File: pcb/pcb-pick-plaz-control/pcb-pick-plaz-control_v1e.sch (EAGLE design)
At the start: 202 parts, among them J1 USB-ID-THT, J3 USB-LCSC_C42431, J3C USB-LCSC_C42431, J3C1 USB-LCSC_C42431, U1 STM32F411VET6, U2 CH340, U3 TPS54227DDAR, U4 SL2.1A, U5 TPS54227DDAR, X1 04-JST-B4B-XH-A, X10 03-JST-B3B-XH-A, X11 03-JST-B3B-XH-A, X12 03-JST-B3B-XH-A, X13 02-JST-B3B-XH-A, X14 02-JST-B3B-XH-A, X15 02-JST-B3B-XH-A, X16 02-JST-B3B-XH-A, X17 02-JST-B3B-XH-A, X18 02-JST-B3B-XH-A, X19 05-JST-B5B-XH-A, X2 04-JST-B4B-XH-A, X20 05-JST-B5B-XH-A, X21 04-JST-B4B-XH-A, X22 PIN_2X13.81MM_LONGPAD, X23 02-JST-B3B-XH-A, X24 02-JST-B3B-XH-A, X25 04-JST-B4B-XH-A, X26 05-JST-B5B-XH-A, X27 05-JST-B5B-XH-A, X28 05-JST-B5B-XH-A, X29 02-JST-B3B-XH-A, X3 04-JST-B4B-XH-A, X30 02-JST-B3B-XH-A, X31 02-JST-B3B-XH-A, X32 02-JST-B3B-XH-A, X33 04-JST-B4B-XH-A, X4 04-JST-B4B-XH-A, X5 04-JST-B4B-XH-A, X6 04-JST-B4B-XH-A, X7 03-JST-B3B-XH-A, X8 03-JST-B3B-XH-A, X9 03-JST-B3B-XH-A, Y1 3213-QUARZ3225, Y2 3213-QUARZ3225, Y3 3213-QUARZ3225

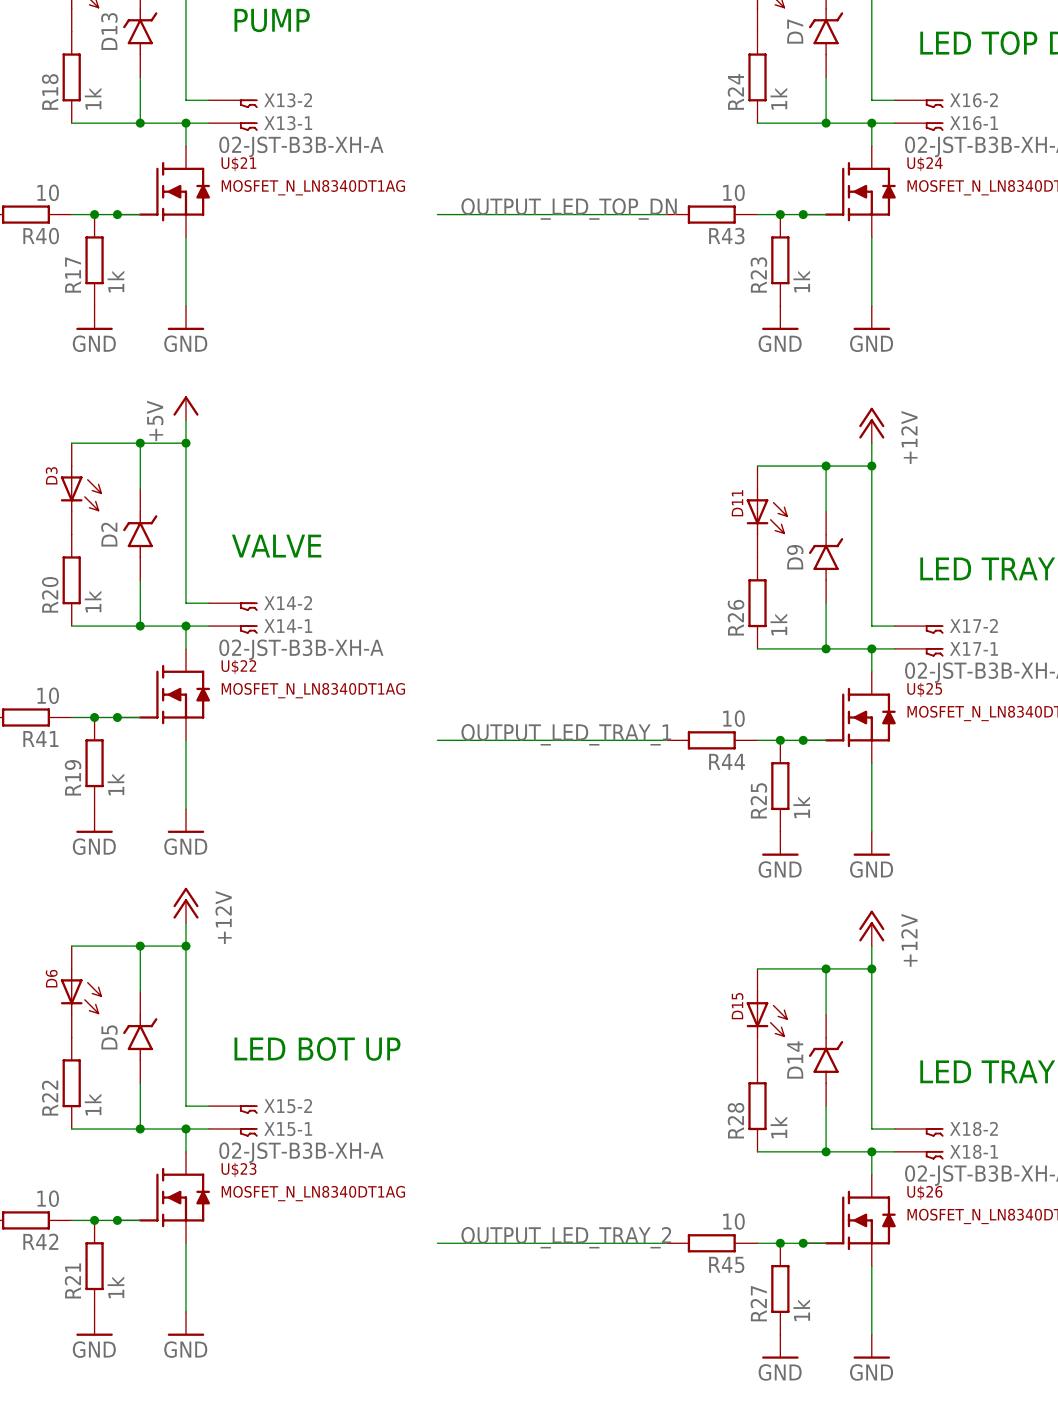
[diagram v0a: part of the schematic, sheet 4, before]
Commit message: updated pcbs with step files
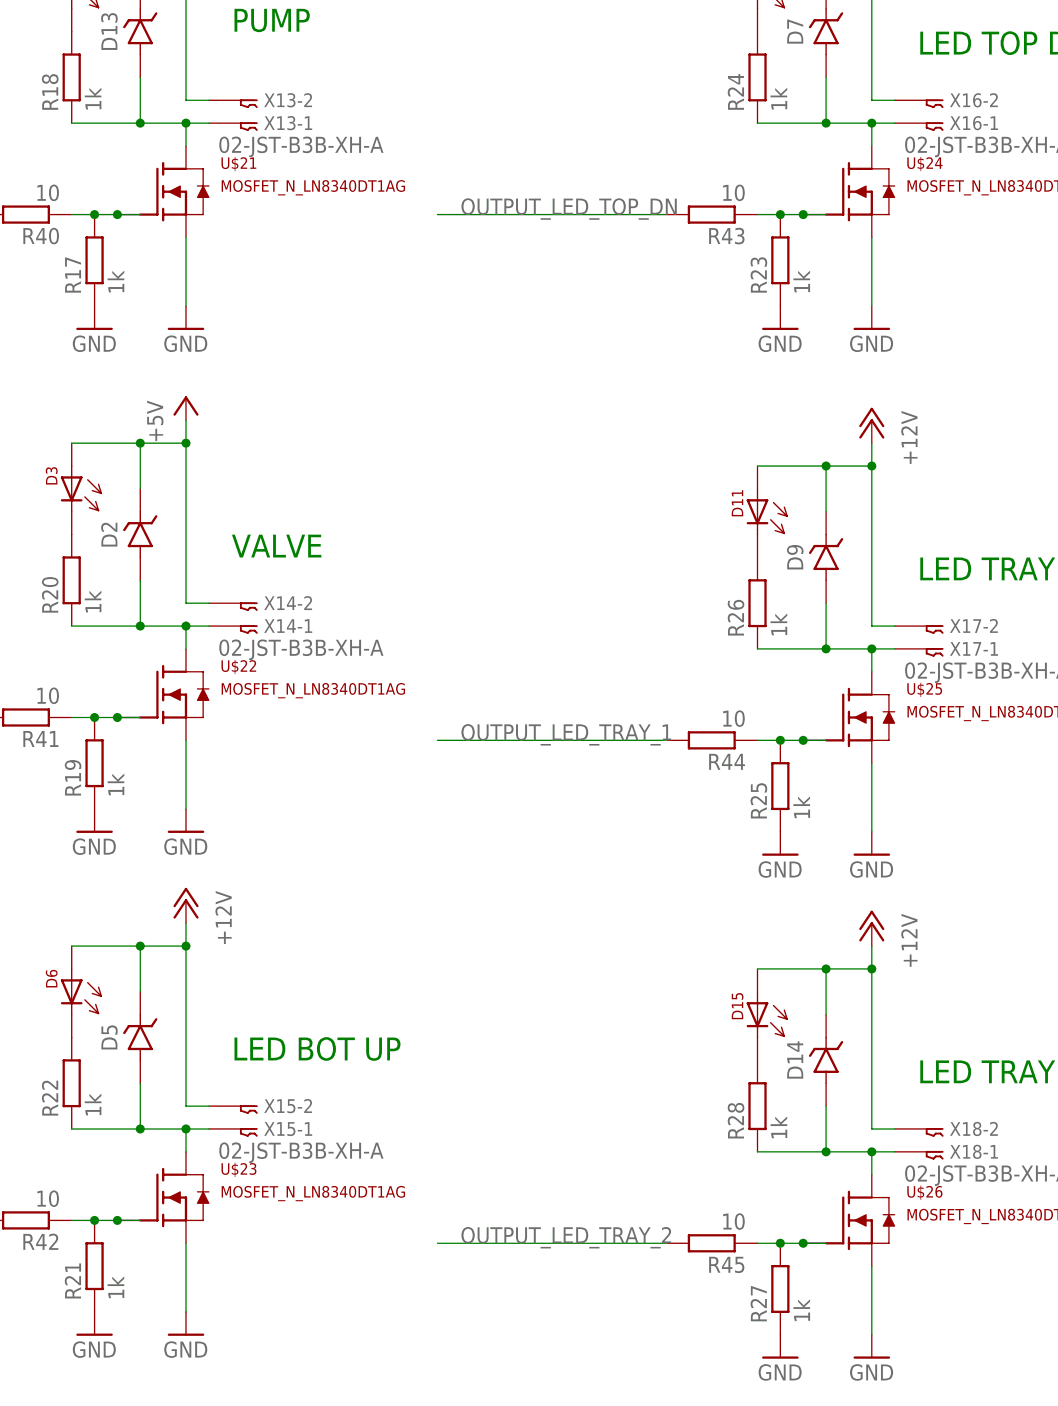
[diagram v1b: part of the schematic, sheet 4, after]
